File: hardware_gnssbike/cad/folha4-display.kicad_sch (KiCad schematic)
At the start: 11 parts, among them J401 Hirose FH12-10S-0.5SH(55), J402 HCTL HC-FPC-05-10-5RLTAG, Q401 DMG1012T-7

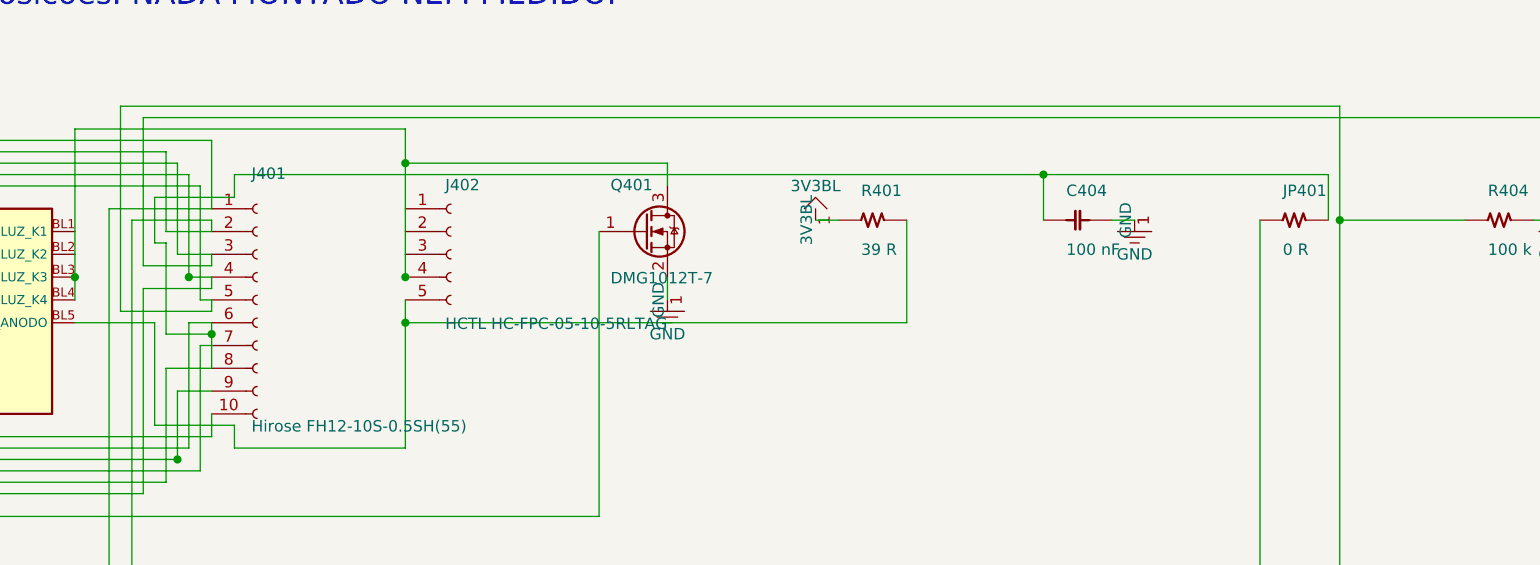
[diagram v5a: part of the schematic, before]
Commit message: feat(hardware): the ERC runs, and 52 hidden errors became 4 deliberate ones
check_sch.py compared our netlist against the one KiCad extracts, pin by
pin, and was good at that and blind to everything else. KiCad's own ERC
had never been run on this schematic. It found 52 errors, and among them
a capacitor with BOTH terminals in the air.

They were of four kinds, and three of them were the drawing failing to
say what it meant rather than the circuit being wrong:

  34 open pins with no flag. The NC pins of the ESD array, the GPIOs
  nobody uses, the receiver's SDA and SCL - it speaks UART - the
  programmer's SWO. Every one of them deliberate, and indistinguishable
  from a forgotten wire. They now carry a no-connect flag, taken from
  nets.py, which is already the source of truth about what is open: a
  pin that appears in no net is open, full stop. A net with a single pin
  counts as open too, which is what R111 became when the harvester
  changed and its pull-up lost its job.

  12 rails with no source the ERC could see. The 1V8_GNSS comes from
  1V8 through a ferrite, the SD3V0_FLASH from SD3V0 through a jumper,
  the harvester's VIN from the panel. PWR_FLAG is the symbol that exists
  to say "this is supplied, I answer for it". One per ELECTRICAL GROUP,
  not per net and not per sheet: two nets that share a pin are one net
  to KiCad - the display connector carries FPC_VSS on one side and GND
  on the other through the same contact - and a flag on each side would
  be two supply outputs wired together, which is another error.

  The last one needed the electrical type to come from the symbol that
  actually reaches the sheet. The four VBUS contacts of the USB-C are
  power_out in our parts.py and passive in KiCad's symbol, so the rule
  believed the rail had a source when it had none.

What is left is four violations, and all four are the same thing: two
supply OUTPUTS wired together. KiCad calls that an error by default
because in signal circuitry two outputs on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
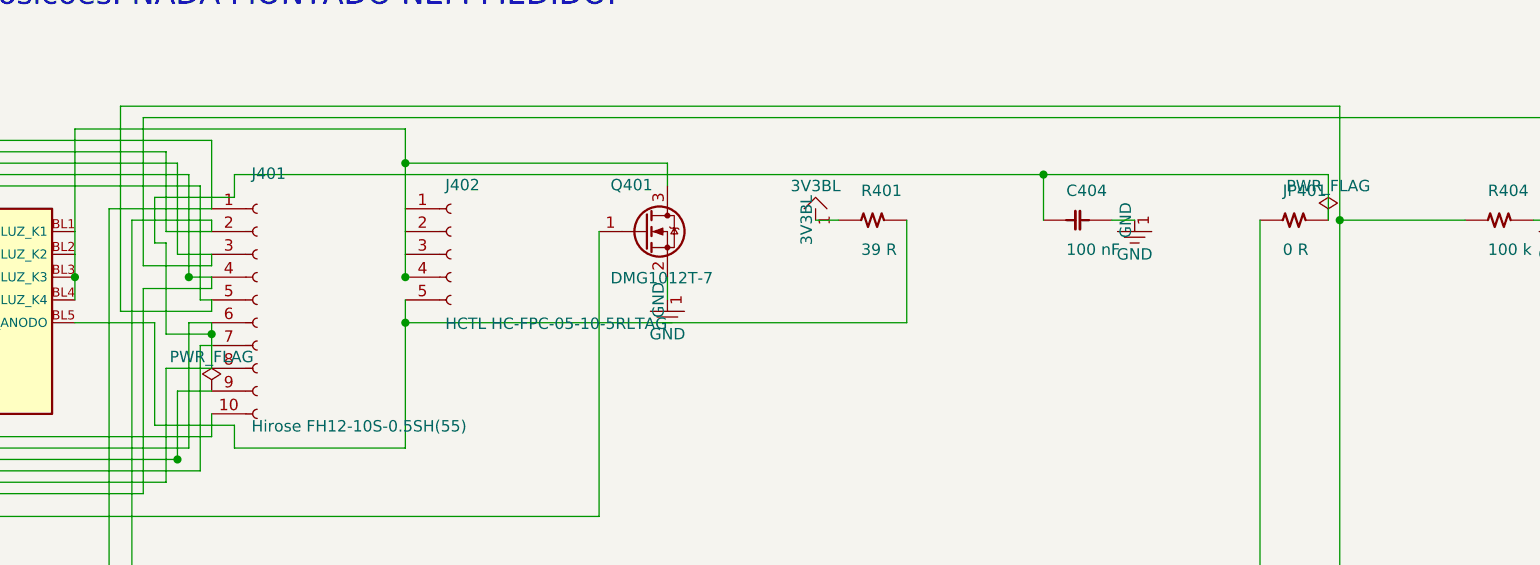
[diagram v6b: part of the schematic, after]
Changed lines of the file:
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@@
+		)
+	)
+	(symbol
+		(lib_id "power:PWR_FLAG")
+		(at 204.470 35.560 0)
+		(unit 1)
+		(exclude_from_sim no)
+		(in_bom no)
+		(on_board yes)
+		(dnp no)
+		(property "Reference" "#FLG010"
+			(at 204.47 35.56 0)
+			(effects (font (size 1.27 1.27)) (hide yes))
+		)
+		(property "Value" "PWR_FLAG"
+			(at 204.470 31.750 0)
+			(effects (font (size 1.27 1.27)))
+		)
+		(property "Footprint" ""
+			(at 204.47 35.56 0)
+			(effects (font (size 1.27 1.27)) (hide yes))
+		)
+		(property "Datasheet" ""
+			(at 204.47 35.56 0)
+			(effects (font (size 1.27 1.27)) (hide yes))
+		)
+		(pin "1")
+		(instances
+			(project "gnssbike"
+				(path "/9c874366-f223-4aef-8b18-3e2a2bab2b25/95879dbd-9df4-46a9-8947-65d27260827b"
+					(reference "#FLG010")
+					(unit 1)
+				)
+			)
+		)
+	)
+	(symbol
+		(lib_id "power:PWR_FLAG")
+		(at 80.010 54.610 0)
+		(unit 1)
+		(exclude_from_sim no)
+		(in_bom no)
+		(on_board yes)
+		(dnp no)
+		(property "Reference" "#FLG011"
+			(at 80.01 54.61 0)
+			(effects (font (size 1.27 1.27)) (hide yes))
+		)
+		(property "Value" "PWR_FLAG"
+			(at 80.010 50.800 0)
+			(effects (font (size 1.27 1.27)))
+		)
+		(property "Footprint" ""
+			(at 80.01 54.61 0)
+			(effects (font (size 1.27 1.27)) (hide yes))
+		)
+		(property "Datasheet" ""
+			(at 80.01 54.61 0)
+			(effects (font (size 1.27 1.27)) (hide yes))
+		)
+		(pin "1")
+		(instances
+			(project "gnssbike"
+				(path "/9c874366-f223-4aef-8b18-3e2a2bab2b25/95879dbd-9df4-46a9-8947-65d27260827b"
+					(reference "#FLG011")
+					(unit 1)
+				)
+			)
 		)
 	)

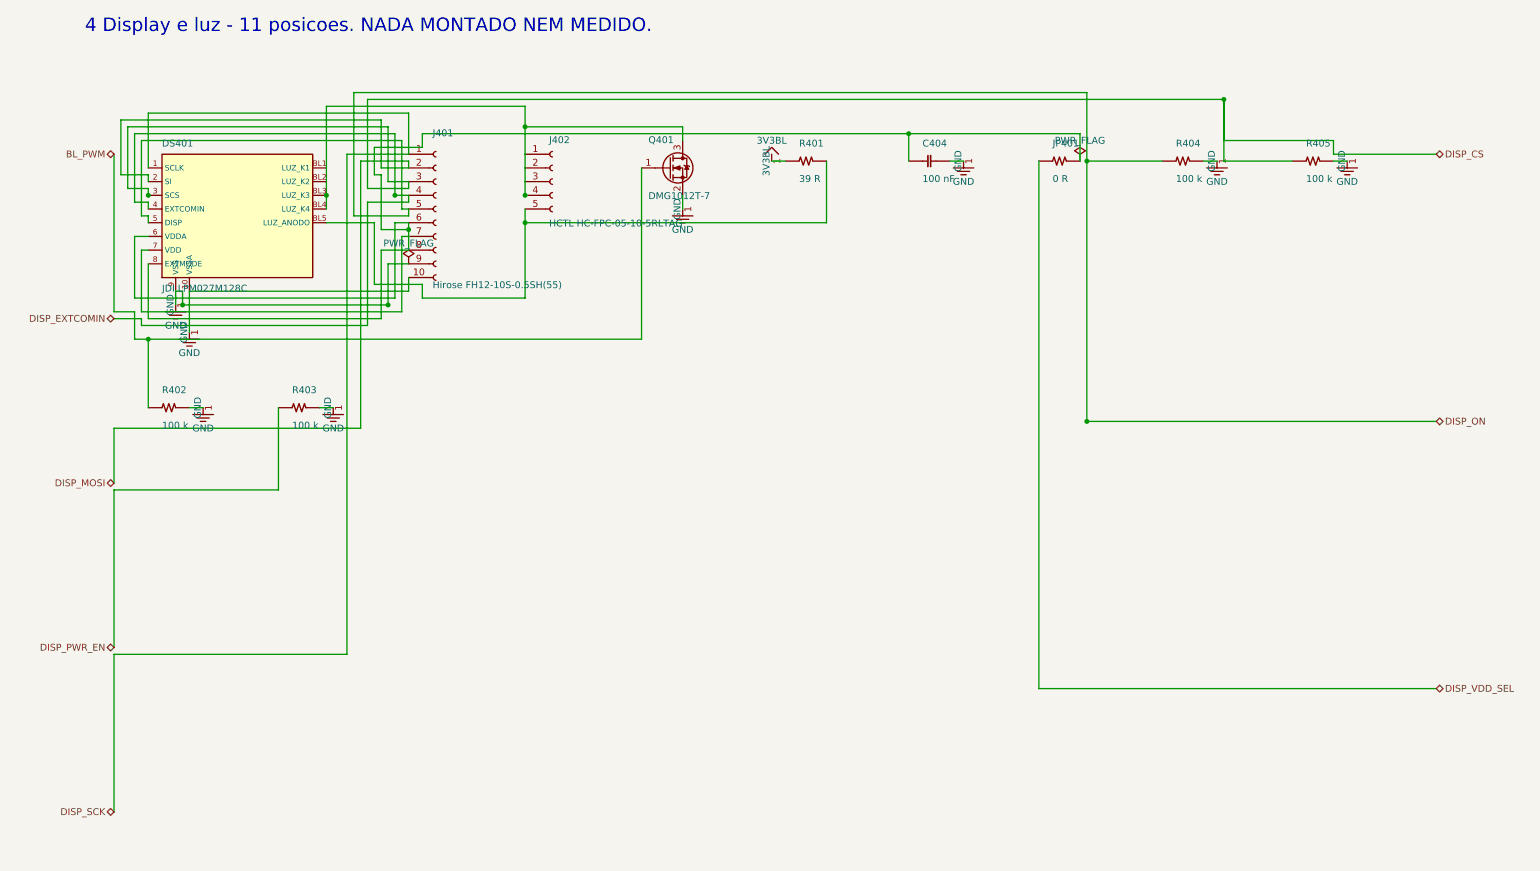
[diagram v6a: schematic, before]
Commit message: feat(hardware): GNSS receiver on the 3V0 rail, and the electrical items closed with the owner
The receiver ran at 1.8 V from BUCK1 through a TXU0204 level shifter, and
table 35 of the MAX-F10S integration manual asks +-2 % of a 1.8 V supply
where the nPM1300 buck gives +-5 %. A +-1 % LDO from 3V0 fixed the
tolerance and cost 35 mW at the battery (the receiver paid at 3.0 V with
1.2 V burnt in the LDO); option 1 of the same table - VCC and V_IO tied at
3.0 V, VIO_SEL open - costs 11 mW and removes the shifter. The owner chose
option 1. The receiver now sits on 3V0 through JP103 and the ferrite, the
four digital lines go pin to pin, the shifter and the LDO leave with four
capacitors, and BUCK1 stays fitted and unloaded as in configuration 1 of
the nPM1300 datasheet (the datasheet only shows an unused BUCK2, and what
it does not show is not copied). The devicetree follows: vcc-supply on
BUCK2, BUCK1 regulator-boot-off. The receiver no longer has a rail that
switches off; that consequence is recorded in docs/10.

Closed the same day, each a decision of the owner or a datasheet fact:

  - the ADP5091 TERM and SETSD dividers hung from BAT with REF open;
    figure 42 of the datasheet hangs all four external dividers from REF,
    which the chip switches to BAT with the hysteresis resistor in series.
    Equation 6 did not hold as drawn. Net ADP_REF, same values.
  - the solar charge thermal cut-off: the ADP5091 has no temperature
    input and the NTC divider was on the board with nobody reading it. A
    TLV7031 fed from the panel compares RT101/R106 with half of SRC and
    pulls DIS_SW high through a BAT54WS, in diode-OR with the USB divider.
    Hot side only; charging below 0 C stays open, and says so.
  - the centre key reaches P1.27 through a Schottky (D107): the SHPHLD
    node rises to 5.5 V with the cable.
  - J102 copper matched to the pinout 06 sends to the pack maker: the
    copper had VBAT+ on 1, NTC on 4, GND on 6 and 2, 3 and 5 open.
  - FB301 with 150 mO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
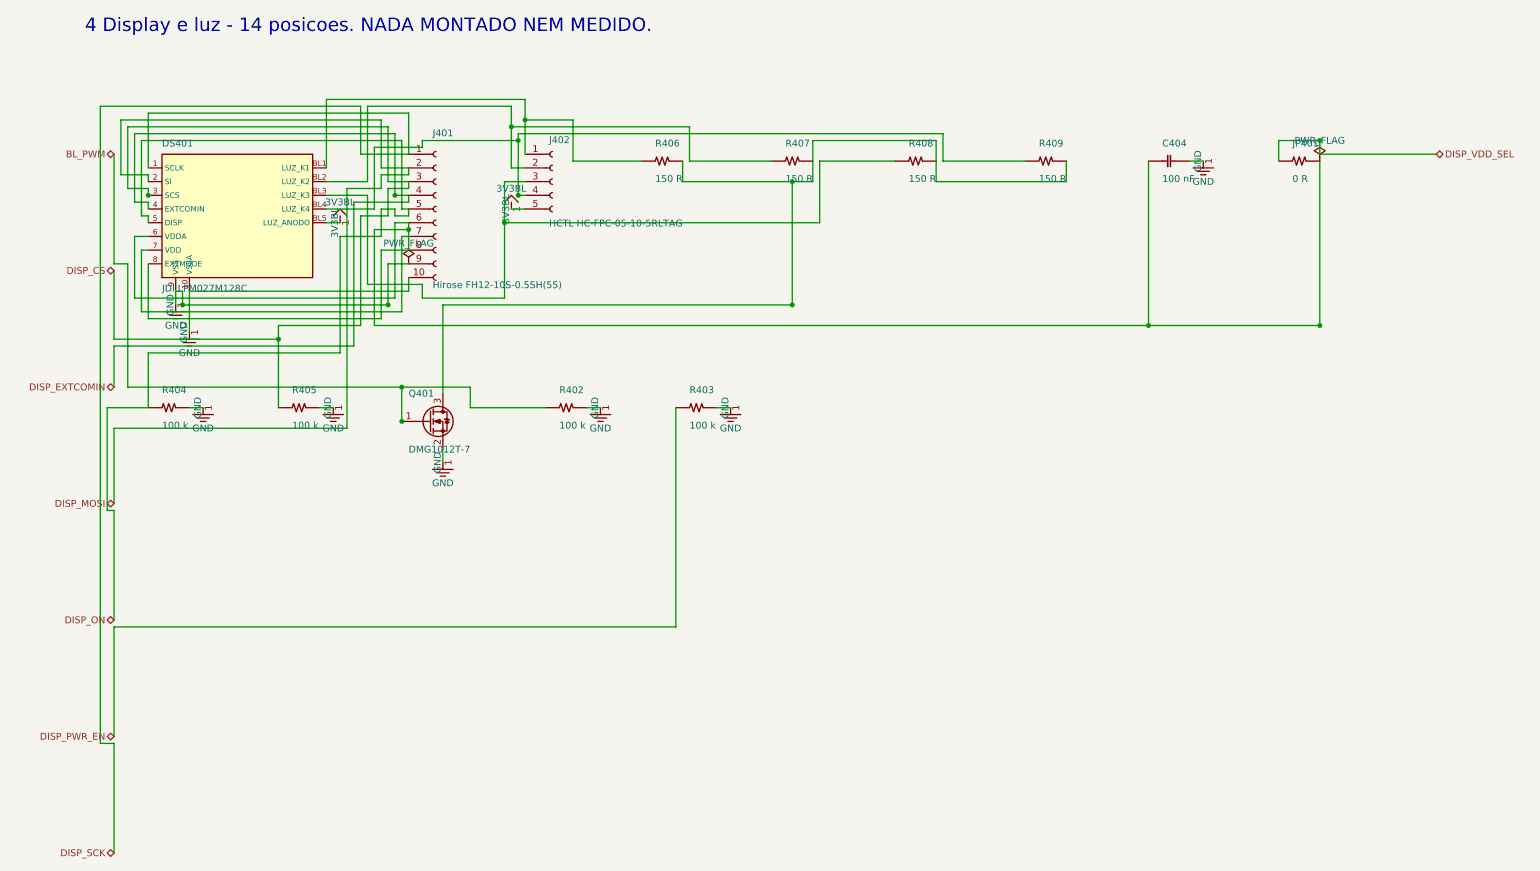
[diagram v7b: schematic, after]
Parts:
- removed R401: 39 R, Resistor_SMD:R_0402_1005Metric, symbol gnssbike:R401
- added R406: 150 R, Resistor_SMD:R_0402_1005Metric, symbol gnssbike:R406
- added R407: 150 R, Resistor_SMD:R_0402_1005Metric, symbol gnssbike:R407
- added R408: 150 R, Resistor_SMD:R_0402_1005Metric, symbol gnssbike:R408
- added R409: 150 R, Resistor_SMD:R_0402_1005Metric, symbol gnssbike:R409
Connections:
- net 3V3BL: now also DS401.BL5 (LUZ_ANODO), J402.5 (Pin_5)
- new net: DS401.BL2 (LUZ_K2), J402.2 (Pin_2), R407.1
- new net: Q401.3 (D), R406.2, R407.2, R408.2, R409.2
- new net: DS401.BL4 (LUZ_K4), J402.4 (Pin_4), R409.1
- new net: DS401.BL3 (LUZ_K3), J402.3 (Pin_3), R408.1
- new net: DS401.BL1 (LUZ_K1), J402.1 (Pin_1), R406.1
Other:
- note added: "4 Display e luz - 14 posicoes. NADA MONTADO NEM MEDIDO."
- note removed: "4 Display e luz - 11 posicoes. NADA MONTADO NEM MEDIDO."
- moved on the sheet: C404, JP401, Q401, R402, R403, R404, R405

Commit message: feat(hardware): draw the schematic by functional block, the way a person reads it
The owner asked for an industrial-standard schematic: wires and labels,
A4 or A3 pages, the right symbols and values, easy to read, the circuits
subdivided by dashed boxes. Until now each sheet was the netlist drawn as
wires - parts on a grid in connection order and a maze router pulling a
wire from every pin to wherever its other end was, across the page.

blocos.py turns each sheet into a row of functional blocks in the order
the signal flows, each in a dashed rectangle with a title: on the power
sheet, USB-C and protection, the nPM1300, the gauge and the cell, the GNSS
backup, the solar harvester, the thermal cut-off. Membership comes from
the BLOCOS table (the anchors), then make_pcb.DECOPLA and JUNTO (the
board already says whose each capacitor is), then sheets.SEGUE, then the
netlist without rails, nearest anchor by hops. Inside a block the anchor
sits in the middle and each passive beside the pin it serves, on the
side that pin faces, mirrored when the pin that serves the chip is the
far one; parts that touch only rails go to a shelf under the chip. Rails
are power symbols, neighbouring pins of one rail get a wire along their
tips and one symbol; a net that leaves its block is a local label, one
that leaves the sheet a hierarchical label, both on a short stub the
maze router bends when the straight way is taken. Sheet 1 is A3, the
rest A4, measured by the drawing itself. Decoupling capacitors now live
on their chip's sheet whatever their number.

Three KiCad 8 facts were measured with kicad-cli's netlist export on the
way, because the first version assumed each one wrong and check_sch.py
caught it: (mirror x) swaps left for right, not (mirror y); a local label
named after a rail is the net /sheet/RAIL, another net; and a pin in the
middle of a long wire is not on it - "wires connect with other wires or
pins only if their ends coincide exactly" (Eeschema manual). The
conventions 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
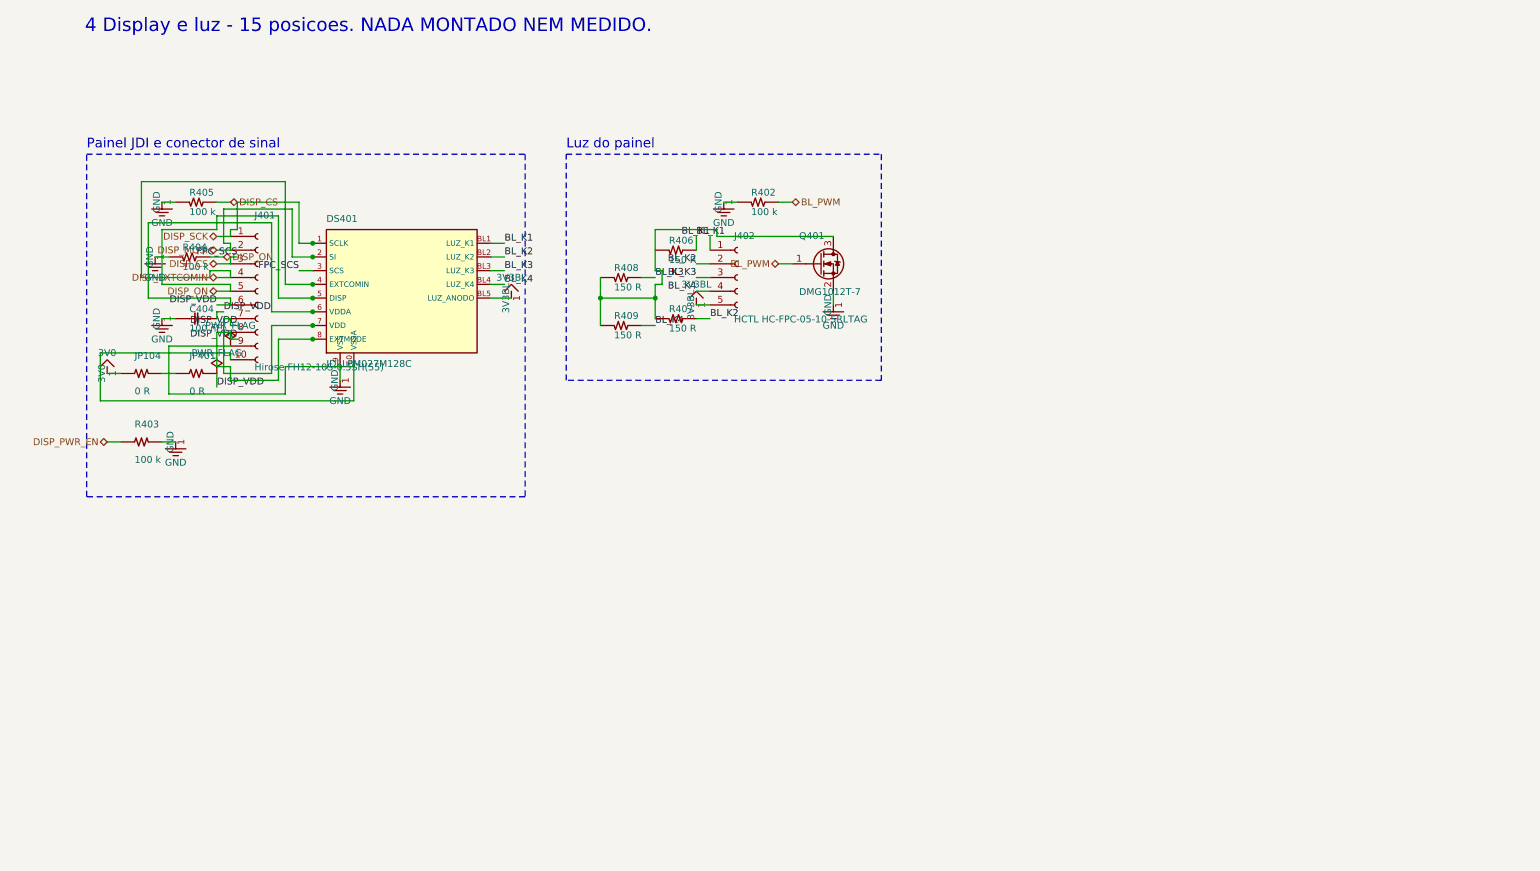
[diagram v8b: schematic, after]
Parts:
- added JP104: 0 R, Resistor_SMD:R_0402_1005Metric, symbol gnssbike:JP104
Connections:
- net BL_K2: now reaches DS401.BL2 (LUZ_K2), J402.2 (Pin_2), R407.1
- net BL_K4: now reaches DS401.BL4 (LUZ_K4), J402.4 (Pin_4), R409.1
- net DISP_VDD: now reaches C404.1, DS401.6 (VDDA), DS401.7 (VDD), DS401.8 (EXTMODE), J401.6 (Pin_6), J401.7 (Pin_7), J401.8 (Pin_8), JP401.2
- net BL_K3: now reaches DS401.BL3 (LUZ_K3), J402.3 (Pin_3), R408.1
- net BL_K1: now reaches DS401.BL1 (LUZ_K1), J402.1 (Pin_1), R406.1
- net DISP_VDD_SEL: no longer names the net of JP401.1
- net DISP_VDD_SEL: now also JP104.2
- new net 3V0: JP104.1
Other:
- note added: "4 Display e luz - 15 posicoes. NADA MONTADO NEM MEDIDO."
- note added: "Luz do painel"
- note added: "Painel JDI e conector de sinal"
- note removed: "4 Display e luz - 14 posicoes. NADA MONTADO NEM MEDIDO."
- moved on the sheet: C404, DS401, J401, J402, JP401, Q401, R402, R403, R404, R405, R406, R407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
